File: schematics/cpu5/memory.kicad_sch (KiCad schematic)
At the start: 0 parts

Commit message: Multithread + paging!
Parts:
- added INTERNAL_ADDRESS_CONN2: Conn_01x16, Connector_PinHeader_2.54mm:PinHeader_1x16_P2.54mm_Vertical, symbol Connector_Generic:Conn_01x16
- added INTERNAL_DATA_CONN4, INTERNAL_DATA_CONN5: Conn_01x08, Connector_PinHeader_2.54mm:PinHeader_1x08_P2.54mm_Vertical, symbol Connector_Generic:Conn_01x08
- added ML8: 74LS574, Package_DIP:DIP-20_W7.62mm, symbol 7400_ice:74LS574
- added U100: CY62256-70PC, Package_DIP:DIP-28_W15.24mm, symbol Memory_RAM:CY62256-70PC
- added U101: 74LS04, Package_DIP:DIP-14_W7.62mm, symbol 7400_ice:74LS04
- added U102, U108: 74LS02, Package_DIP:DIP-14_W7.62mm, symbol 7400_ice:74LS02
- added U103, U104, U105, U106, U107, U115, U116, U118, U119, U94: 74LS541, Package_DIP:DIP-20_W7.62mm, symbol 7400_ice:74LS541
- added U109, U112, U113, U95: 74LS32, Package_DIP:DIP-14_W7.62mm, symbol 7400_ice:74LS32
- added U110, U111: AT28C64-20PI, Package_DIP:DIP-28_W7.62mm, symbol at28c64:AT28C64-20PI
- added U114, U117, U96: 74LS138, Package_DIP:DIP-16_W7.62mm, symbol 7400_ice:74LS138
- added U120: AS6C4008-55PCN, Package_DIP:DIP-32_W15.24mm, symbol Memory_RAM:AS6C4008-55PCN
- added U97: 74LS00, Package_DIP:DIP-14_W7.62mm, symbol 7400_ice:74LS00
- added U98: 28C256, Package_DIP:DIP-28_W15.24mm, symbol Memory_EEPROM:28C256
- added U99: 74LS08, Package_DIP:DIP-14_W7.62mm, symbol 7400_ice:74LS08
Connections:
- new net: U95.3 (Y1), U95.9 (A3)
- new net: U101.5 (A2), U95.13 (B4), U95.8 (Y3), U96.5 (Enable2_bar)
- new net: U95.10 (B3), U95.6 (Y2)
- new net: U109.3 (Y1), U112.13 (B4), U112.9 (A3)
- new net: U101.2 (Y0), U95.12 (A4)
- new net: U110.22 (/OE), U99.8 (Y3)
- new net: U102.5 (A2), U109.8 (Y3)
- new net: U109.10 (B3), U109.11 (Y4)
- new net: U109.6 (Y2), U112.1 (A1), U112.5 (B2)
- new net: U109.2 (B1), U109.5 (B2), U96.12 (Y3)
- new net: U114.5 (Enable2_bar), U96.13 (Y2)
- new net: U96.14 (Y1), U99.2 (B1)
- new net: U96.15 (Y0), U99.1 (A1)
- new net: U108.1 (Y1), U113.2 (B1)
- new net: U102.9 (B3), U113.3 (Y1)
- new net: U102.13 (Y4), U109.13 (B4)
- new net: U114.13 (Y2), U117.5 (Enable2_bar)
- new net: U115.1 (OE1_bar), U97.6 (Y2)
- new net: U101.12 (Y5), U109.4 (A2)
- new net: U111.22 (/OE), U99.6 (Y2)
- new net: U116.1 (OE1_bar), U97.11 (Y4)
- new net: ML8.11 (CLK), U102.1 (Y1)
- new net +5V: ML8.20 (VCC), U100.28 (VCC), U101.14 (VCC), U102.14 (VCC), U103.20 (VCC), U104.20 (VCC), U105.20 (VCC), U106.20 (VCC), U107.20 (VCC), U108.14 (VCC), U109.14 (VCC), U110.28 (VCC), U111.28 (VCC), U112.14 (VCC), U113.14 (VCC), U114.16 (VCC), U114.6 (Enable3), U115.20 (VCC), U116.20 (VCC), U117.16 (VCC), U117.6 (Enable3), U118.20 (VCC), U119.20 (VCC), U120.32 (VCC), U94.20 (VCC), U95.14 (VCC), U96.16 (VCC), U96.6 (Enable3), U97.14 (VCC), U98.27 (~{WE}), U98.28 (VCC), U99.14 (VCC)
- new net ADDR0: INTERNAL_ADDRESS_CONN2.1 (Pin_1), U100.10 (A0), U104.2 (A0), U117.1 (A0), U120.12 (A0), U98.10 (A0)
- new net ADDR1: INTERNAL_ADDRESS_CONN2.2 (Pin_2), U100.9 (A1), U104.3 (A1), U117.2 (A1), U120.11 (A1), U98.9 (A1)
- new net ADDR10: INTERNAL_ADDRESS_CONN2.11 (Pin_11), U100.21 (A10), U105.4 (A2), U114.1 (A0), U120.23 (A10), U98.21 (A10)
- new net ADDR11: INTERNAL_ADDRESS_CONN2.12 (Pin_12), U100.23 (A11), U105.5 (A3), U114.2 (A1), U120.25 (A11), U98.23 (A11)
- new net ADDR12: INTERNAL_ADDRESS_CONN2.13 (Pin_13), U101.13 (A5), U106.2 (A0), U109.1 (A1), U94.2 (A0)
- new net ADDR13: INTERNAL_ADDRESS_CONN2.14 (Pin_14), U106.3 (A1), U94.3 (A1)
- new net ADDR14: INTERNAL_ADDRESS_CONN2.15 (Pin_15), U106.4 (A2), U94.4 (A2)
- new net ADDR15: INTERNAL_ADDRESS_CONN2.16 (Pin_16), U106.5 (A3), U94.5 (A3)
- new net ADDR2: INTERNAL_ADDRESS_CONN2.3 (Pin_3), U100.8 (A2), U104.4 (A2), U117.3 (A2), U120.10 (A2), U98.8 (A2)
- new net ADDR3: INTERNAL_ADDRESS_CONN2.4 (Pin_4), U100.7 (A3), U104.5 (A3), U120.9 (A3), U98.7 (A3)
- new net ADDR4: INTERNAL_ADDRESS_CONN2.5 (Pin_5), U100.6 (A4), U104.6 (A4), U120.8 (A4), U98.6 (A4)
- new net ADDR5: INTERNAL_ADDRESS_CONN2.6 (Pin_6), U100.5 (A5), U104.7 (A5), U120.7 (A5), U98.5 (A5)
- new net ADDR6: INTERNAL_ADDRESS_CONN2.7 (Pin_7), U100.4 (A6), U104.8 (A6), U120.6 (A6), U98.4 (A6)
- new net ADDR7: INTERNAL_ADDRESS_CONN2.8 (Pin_8), U100.3 (A7), U104.9 (A7), U120.5 (A7), U98.3 (A7)
- new net ADDR8: INTERNAL_ADDRESS_CONN2.9 (Pin_9), U100.25 (A8), U105.2 (A0), U120.27 (A8), U98.25 (A8)
- new net ADDR9: INTERNAL_ADDRESS_CONN2.10 (Pin_10), U100.24 (A9), U105.3 (A1), U120.26 (A9), U98.24 (A9)
- new net DATA0: INTERNAL_DATA_CONN4.1 (Pin_1), ML8.2 (D0), U100.11 (D0), U115.2 (A0), U116.2 (A0), U118.18 (Y0), U119.18 (Y0), U120.13 (D0), U98.11 (D0)
- new net DATA1: INTERNAL_DATA_CONN4.2 (Pin_2), ML8.3 (D1), U100.12 (D1), U115.3 (A1), U116.3 (A1), U118.17 (Y1), U119.17 (Y1), U120.14 (D1), U98.12 (D1)
- new net DATA2: INTERNAL_DATA_CONN4.3 (Pin_3), ML8.4 (D2), U100.13 (D2), U115.4 (A2), U116.4 (A2), U118.16 (Y2), U119.16 (Y2), U120.15 (D2), U98.13 (D2)
- new net DATA3: INTERNAL_DATA_CONN4.4 (Pin_4), ML8.5 (D3), U100.15 (D3), U115.5 (A3), U116.5 (A3), U118.15 (Y3), U119.15 (Y3), U120.17 (D3), U98.15 (D3)
- new net DATA4: INTERNAL_DATA_CONN4.5 (Pin_5), ML8.6 (D4), U100.16 (D4), U115.6 (A4), U116.6 (A4), U118.14 (Y4), U119.14 (Y4), U120.18 (D4), U98.16 (D4)
- new net DATA5: INTERNAL_DATA_CONN4.6 (Pin_6), ML8.7 (D5), U100.17 (D5), U115.7 (A5), U116.7 (A5), U118.13 (Y5), U119.13 (Y5), U120.19 (D5), U98.17 (D5)
- new net DATA6: INTERNAL_DATA_CONN4.7 (Pin_7), ML8.8 (D6), U100.18 (D6), U115.8 (A6), U116.8 (A6), U118.12 (Y6), U119.12 (Y6), U120.20 (D6), U98.18 (D6)
- new net DATA7: INTERNAL_DATA_CONN4.8 (Pin_8), ML8.9 (D7), U100.19 (D7), U115.9 (A7), U116.9 (A7), U118.11 (Y7), U119.11 (Y7), U120.21 (D7), U98.19 (D7)
- new net DBG_SEL_RAM: U100.20 (~{CS}), U95.11 (Y4)
- new net DBG_SEL_ROM: U98.20 (~{CS}), U99.3 (Y1)
- new net EADDR12: U100.2 (A12), U103.18 (Y0), U114.3 (A2), U120.4 (A12), U94.18 (Y0), U98.2 (A12)
- new net EADDR13: U100.26 (A13), U103.17 (Y1), U120.28 (A13), U94.17 (Y1), U96.1 (A0), U98.26 (A13)
- new net EADDR14: U100.1 (A14), U103.16 (Y2), U120.3 (A14), U94.16 (Y2), U96.2 (A1)
- new net EADDR15: U101.1 (A0), U103.15 (Y3), U120.31 (A15), U94.15 (Y3), U96.3 (A2)
- new net EADDR16: U103.14 (Y4), U120.2 (A16), U94.14 (Y4), U95.1 (A1)
- new net EADDR17: U103.13 (Y5), U120.30 (A17), U94.13 (Y5), U95.2 (B1)
- new net EADDR18: U103.12 (Y6), U120.1 (A18), U94.12 (Y6), U95.4 (A2)
- new net EADDR19: U103.11 (Y7), U94.11 (Y7), U95.5 (B2)
- new net EXTRAM_SEL: U101.6 (Y2), U120.22 (~{CE})
- new net GND: ML8.10 (GND), U100.14 (GND), U101.7 (GND), U102.7 (GND), U103.10 (GND), U103.19 (OE2_bar), U104.10 (GND), U104.19 (OE2_bar), U105.10 (GND), U105.19 (OE2_bar), U105.6 (A4), U105.7 (A5), U105.8 (A6), U105.9 (A7), U106.10 (GND), U106.19 (OE2_bar), U107.10 (GND), U107.19 (OE2_bar), U107.6 (A4), U107.7 (A5), U107.8 (A6), U107.9 (A7), U108.7 (GND), U109.7 (GND), U110.14 (GND), U110.2 (A12), U110.20 (/CE), U111.14 (GND), U111.2 (A12), U111.20 (/CE), U112.7 (GND), U113.7 (GND), U114.4 (Enable1_bar), U114.8 (GND), U115.10 (GND), U115.19 (OE2_bar), U116.10 (GND), U116.19 (OE2_bar), U117.4 (Enable1_bar), U117.8 (GND), U118.10 (GND), U118.19 (OE2_bar), U119.10 (GND), U119.19 (OE2_bar), U120.16 (VSS), U94.10 (GND), U94.19 (OE2_bar), U94.6 (A4), U94.7 (A5), U94.8 (A6), U94.9 (A7), U95.7 (GND), U96.4 (Enable1_bar), U96.8 (GND), U97.7 (GND), U98.1 (A14), U98.14 (GND), U99.7 (GND)
- new net MREAD: INTERNAL_DATA_CONN5.2 (Pin_2), U100.22 (~{OE}), U112.10 (B3), U112.2 (B1), U120.24 (~{OE}), U98.22 (~{OE})
- new net MWRITE: INTERNAL_DATA_CONN5.1 (Pin_1), U100.27 (~{WE}), U102.12 (B4), U102.2 (A1), U108.3 (B1), U112.12 (A4), U112.4 (A2), U120.29 (~{WE})
- new net PGE: U102.4 (Y2), U102.8 (A3), U104.1 (OE1_bar), U105.1 (OE1_bar), U94.1 (OE1_bar)
- new net PGE_bar: ML8.1 (OE_bar), U102.10 (Y3), U102.6 (B2), U103.1 (OE1_bar), U106.1 (OE1_bar), U107.1 (OE1_bar), U97.13 (B4), U97.5 (B2), U99.10 (B3), U99.5 (B2)
- new net READ_TLB: U112.8 (Y3), U118.1 (OE1_bar), U97.4 (A2), U99.9 (A3)
- new net READ_TLBF: U112.3 (Y1), U119.1 (OE1_bar), U97.12 (A4), U99.4 (A2)
- new net RESET_PAGING_SEL: U102.11 (A4), U117.15 (Y0)
- new net RESET_bar: U109.9 (A3)
- new net SEL_TLB_INDEX: U102.3 (B1), U117.13 (Y2)
- new net SELa_PGdis: INTERNAL_DATA_CONN5.3 (Pin_3), U109.12 (A4)
- new net SET_PAGING_SEL: U108.2 (A1), U117.14 (Y1)
- new net TLBA0: U104.18 (Y0), U106.18 (Y0), U110.10 (A0), U111.10 (A0)
- new net TLBA1: U104.17 (Y1), U106.17 (Y1), U110.9 (A1), U111.9 (A1)
- new net TLBA10: U105.16 (Y2), U107.16 (Y2), U110.21 (A10), U111.21 (A10)
- new net TLBA11: U105.15 (Y3), U107.15 (Y3), U110.23 (A11), U111.23 (A11)
- new net TLBA2: U104.16 (Y2), U106.16 (Y2), U110.8 (A2), U111.8 (A2)
- new net TLBA3: U104.15 (Y3), U106.15 (Y3), U110.7 (A3), U111.7 (A3)
- new net TLBA4: U104.14 (Y4), U106.14 (Y4), U110.6 (A4), U111.6 (A4)
- new net TLBA5: U104.13 (Y5), U106.13 (Y5), U110.5 (A5), U111.5 (A5)
- new net TLBA6: U104.12 (Y6), U106.12 (Y6), U110.4 (A6), U111.4 (A6)
- new net TLBA7: U104.11 (Y7), U106.11 (Y7), U110.3 (A7), U111.3 (A7)
- new net TLBA8: U105.18 (Y0), U107.18 (Y0), U110.25 (A8), U111.25 (A8)
- new net TLBA9: U105.17 (Y1), U107.17 (Y1), U110.24 (A9), U111.24 (A9)
- new net TLBD0: U103.2 (A0), U110.11 (D0), U115.18 (Y0), U118.2 (A0)
- new net TLBD1: U103.3 (A1), U110.12 (D1), U115.17 (Y1), U118.3 (A1)
- new net TLBD2: U103.4 (A2), U110.13 (D2), U115.16 (Y2), U118.4 (A2)
- new net TLBD3: U103.5 (A3), U110.15 (D3), U115.15 (Y3), U118.5 (A3)
- new net TLBD4: U103.6 (A4), U110.16 (D4), U115.14 (Y4), U118.6 (A4)
- new net TLBD5: U103.7 (A5), U110.17 (D5), U115.13 (Y5), U118.7 (A5)
- new net TLBD6: U103.8 (A6), U110.18 (D6), U115.12 (Y6), U118.8 (A6)
- new net TLBD7: U103.9 (A7), U110.19 (D7), U115.11 (Y7), U118.9 (A7)
- new net TLBFD0: U111.11 (D0), U116.18 (Y0), U119.2 (A0)
- new net TLBFD1: U111.12 (D1), U116.17 (Y1), U119.3 (A1)
- new net TLBFD2: U111.13 (D2), U116.16 (Y2), U119.4 (A2)
- new net TLBFD3: U111.15 (D3), U116.15 (Y3), U119.5 (A3)
- new net TLBFD4: U111.16 (D4), U116.14 (Y4), U119.6 (A4)
- new net TLBFD5: U111.17 (D5), U116.13 (Y5), U119.7 (A5)
- new net TLBFD6: U111.18 (D6), U116.12 (Y6), U119.8 (A6)
- new net TLBFD7: U111.19 (D7), U116.11 (Y7), U119.9 (A7)
- new net TLBi0: ML8.19 (Y0), U106.6 (A4)
- new net TLBi1: ML8.18 (Y1), U106.7 (A5)
- new net TLBi2: ML8.17 (Y2), U106.8 (A6)
- new net TLBi3: ML8.16 (Y3), U106.9 (A7)
- new net TLBi4: ML8.15 (Y4), U107.2 (A0)
- new net TLBi5: ML8.14 (Y5), U107.3 (A1)
- new net TLBi6: ML8.13 (Y6), U107.4 (A2)
- new net TLBi7: ML8.12 (Y7), U107.5 (A3)
- new net WRITE_TLB: U110.27 (/WE), U112.11 (Y4)
- new net WRITE_TLBF: U111.27 (/WE), U112.6 (Y2)
- new net ei: INTERNAL_DATA_CONN5.4 (Pin_4), U113.1 (A1)
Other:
- note added: "0x0000-0x3fff"
- note added: "0x4000-0x5fff"
- note added: "0x4800"
- note added: "0x4800-0x4bff"
- note added: "0x4801"
- note added: "0x4802"
- note added: "0x6000-0x7fff"

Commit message: start faults
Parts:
- added ML10, ML11, ML9: 74LS574, Package_DIP:DIP-20_W7.62mm, symbol 7400_ice:74LS574
- added U121: 74LS32, Package_DIP:DIP-14_W7.62mm, symbol 7400_ice:74LS32
- added U123: 74LS08, Package_DIP:DIP-14_W7.62mm, symbol 7400_ice:74LS08
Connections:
- net +5V: now also ML10.20 (VCC), ML11.20 (VCC), ML9.20 (VCC), U121.14 (VCC), U123.14 (VCC)
- net ADDR0: now also ML9.2 (D0)
- net ADDR1: now also ML9.3 (D1)
- net ADDR10: now also ML10.4 (D2)
- net ADDR11: now also ML10.5 (D3)
- net ADDR2: now also ML9.4 (D2)
- net ADDR3: now also ML9.5 (D3)
- net ADDR4: now also ML9.6 (D4)
- net ADDR5: now also ML9.7 (D5)
- net ADDR6: now also ML9.8 (D6)
- net ADDR7: now also ML9.9 (D7)
- net ADDR8: now also ML10.2 (D0)
- net ADDR9: now also ML10.3 (D1)
- net DATA0: now also ML10.19 (Y0), ML11.19 (Y0), ML9.19 (Y0)
- net DATA1: now also ML10.18 (Y1), ML11.18 (Y1), ML9.18 (Y1)
- net DATA2: now also ML10.17 (Y2), ML11.17 (Y2), ML9.17 (Y2)
- net DATA3: now also ML10.16 (Y3), ML11.16 (Y3), ML9.16 (Y3)
- net DATA4: now also ML10.15 (Y4), ML11.15 (Y4), ML9.15 (Y4)
- net DATA5: now also ML10.14 (Y5), ML11.14 (Y5), ML9.14 (Y5)
- net DATA6: now also ML10.13 (Y6), ML11.13 (Y6), ML9.13 (Y6)
- net DATA7: now also ML10.12 (Y7), ML11.12 (Y7), ML9.12 (Y7)
- net EADDR12: now also ML10.6 (D4)
- net EADDR13: now also ML10.7 (D5)
- net EADDR14: now also ML10.8 (D6)
- net EADDR15: now also ML10.9 (D7)
- net EADDR16: now also ML11.2 (D0)
- net EADDR17: now also ML11.3 (D1)
- net EADDR18: now also ML11.4 (D2)
- net EADDR19: now also ML11.5 (D3)
- net GND: now also ML8.1 (OE_bar), ML10.10 (GND), ML11.10 (GND), ML9.10 (GND), U121.7 (GND), U123.7 (GND)
- net MREAD: now also U108.12 (B4), U121.10 (B3), U121.12 (A4), U121.2 (B1), U121.5 (B2); no longer U100.22 (~{OE}), U120.24 (~{OE}), U98.22 (~{OE})
- net MWRITE: now also U108.6 (B2), U113.12 (A4); no longer U100.27 (~{WE}), U120.29 (~{WE})
- net PGE: now also U99.13 (B4), U123.2 (B1)
- net PGE_bar: no longer ML8.1 (OE_bar)
- net TLBFD0: now also U108.11 (A4), ML11.6 (D4)
- net TLBFD1: now also U108.5 (A2), ML11.7 (D5)
- net TLBFD2: now also ML11.8 (D6)
- net TLBFD3: now also ML11.9 (D7)
- net at U108.4 (Y2): now also U99.12 (A4)
- net at U99.11 (Y4): now also U113.10 (B3), U113.13 (B4)
- net MWRITE_f: now reaches U113.11 (Y4)
- net MWRITE_f: now also U100.27 (~{WE}), U120.29 (~{WE})
- net RD_FLT_1: now reaches U117.10 (Y5)
- net RD_FLT_1: now also U121.9 (A3)
- net RD_FLT_0: now reaches U117.11 (Y4)
- net RD_FLT_0: now also U121.4 (A2)
- net RD_FLT_2: now reaches U117.9 (Y6)
- net RD_FLT_2: now also U121.1 (A1)
- net at U108.13 (Y4): now also U123.1 (A1)
- net MMU_FAULT: now reaches U113.9 (A3)
- net MMU_FAULT: now also ML10.11 (CLK), ML11.11 (CLK), ML9.11 (CLK), U121.13 (B4), U123.3 (Y1)
- new net: ML10.1 (OE_bar), U121.8 (Y3)
- new net: ML11.1 (OE_bar), U121.3 (Y1)
- new net: ML9.1 (OE_bar), U121.6 (Y2)
- new net MREAD_f: U100.22 (~{OE}), U120.24 (~{OE}), U121.11 (Y4), U98.22 (~{OE})
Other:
- note added: "0x4803"
- note added: "0x4804"
- note added: "0x4805"
- note added: "0x4806"
- moved on the sheet: U101B, U101D, U101E, U108B, U108D, U113C, U113D, U97C, U99D

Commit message: faults seem to work
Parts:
- added U131: 74LS74, Package_DIP:DIP-14_W7.62mm, symbol 7400_ice:74LS74
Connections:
- net +5V: now also U131.14 (VCC), U131.4 (nS1)
- net GND: now also U131.7 (GND)
- net MMU_FAULT: now also U113.8 (Y3); no longer U113.9 (A3), U121.13 (B4), U123.3 (Y1)
- net PGE: now also U131.5 (Q1); no longer U102.4 (Y2), U102.8 (A3)
- net PGE_bar: now also U131.6 (nQ1); no longer U102.10 (Y3), U102.6 (B2)
- net RD_FLT_0: now also U117.10 (Y5); no longer U117.11 (Y4)
- net RD_FLT_1: now also U117.9 (Y6); no longer U117.10 (Y5)
- net RD_FLT_2: now also U117.7 (Y7); no longer U117.9 (Y6)
- net SET_PAGING_SEL: now also U123.5 (B2), U123.9 (A3)
- net at U113.10 (B3), U113.13 (B4): now also U123.8 (Y3); no longer U99.11 (Y4)
- net at U123.4 (A2): now also U123.3 (Y1)
- net at U123.6 (Y2): now also U113.9 (A3), U121.13 (B4)
- net at U123.10 (B3): now also U99.11 (Y4)
- new net: U102.4 (Y2), U102.8 (A3), U131.2 (D1)
- new net: U102.10 (Y3), U102.6 (B2)
- new net RESET: U131.1 (nR1)
- new net start_phase: U131.3 (Clk1)
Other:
- note added: "0x4807"
- moved on the sheet: U101B, U101D, U101E, U108B, U108D, U113C, U113D, U121D, U123A, U123B, U123C, U123D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

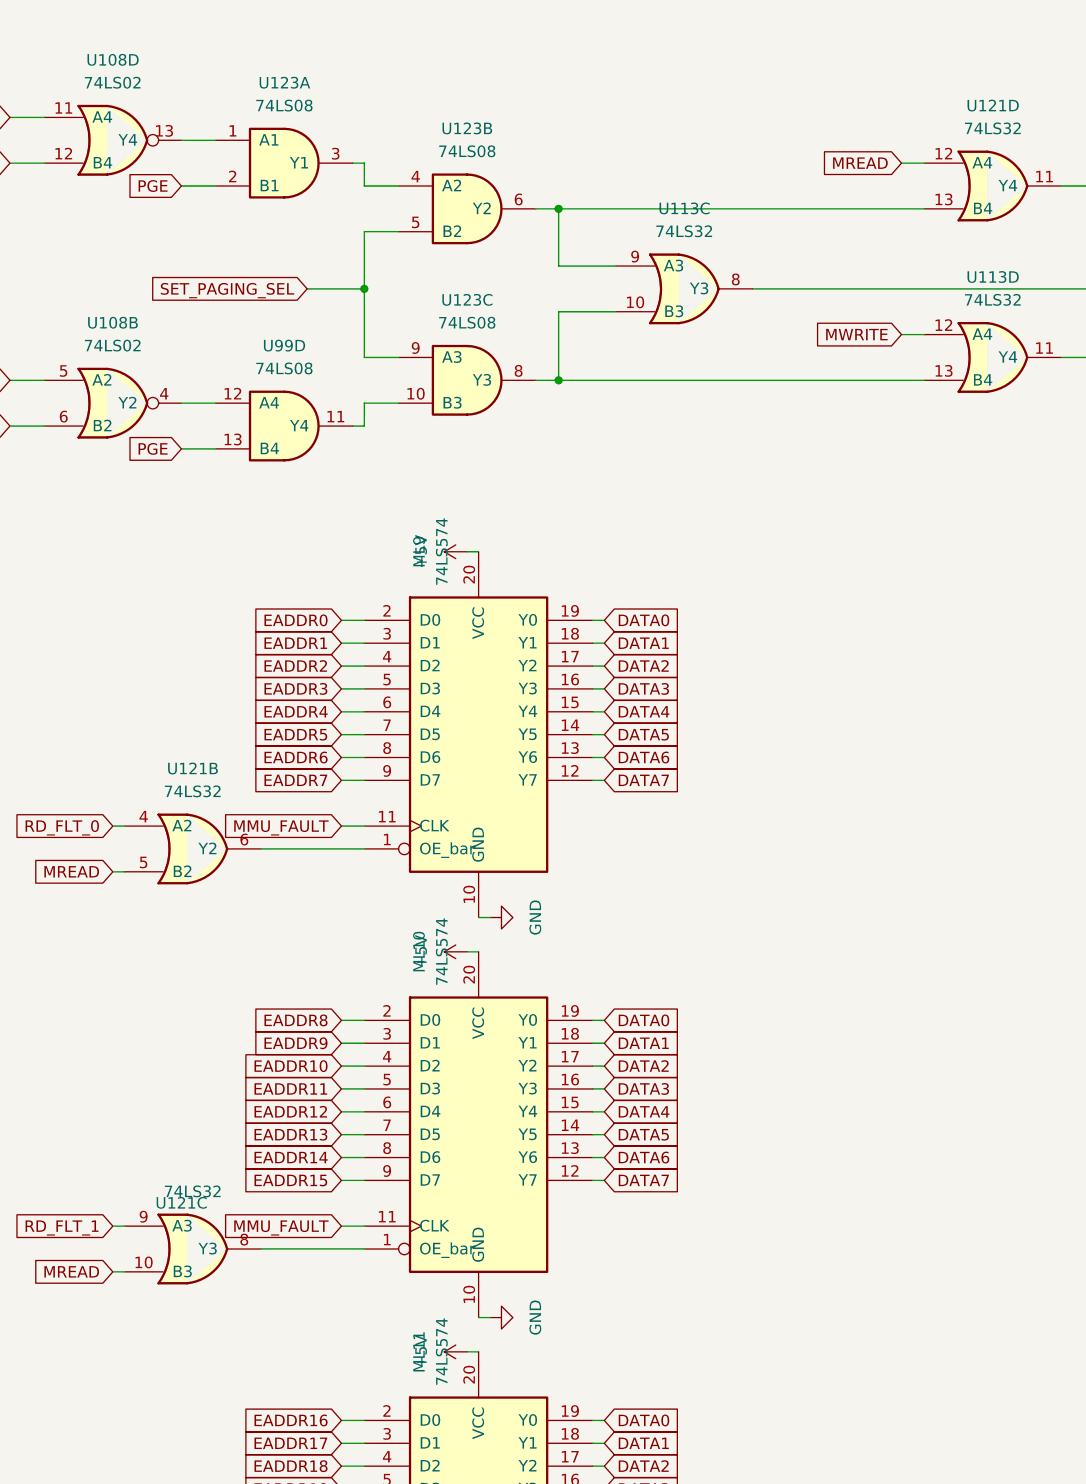
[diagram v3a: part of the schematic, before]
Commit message: Page faults work
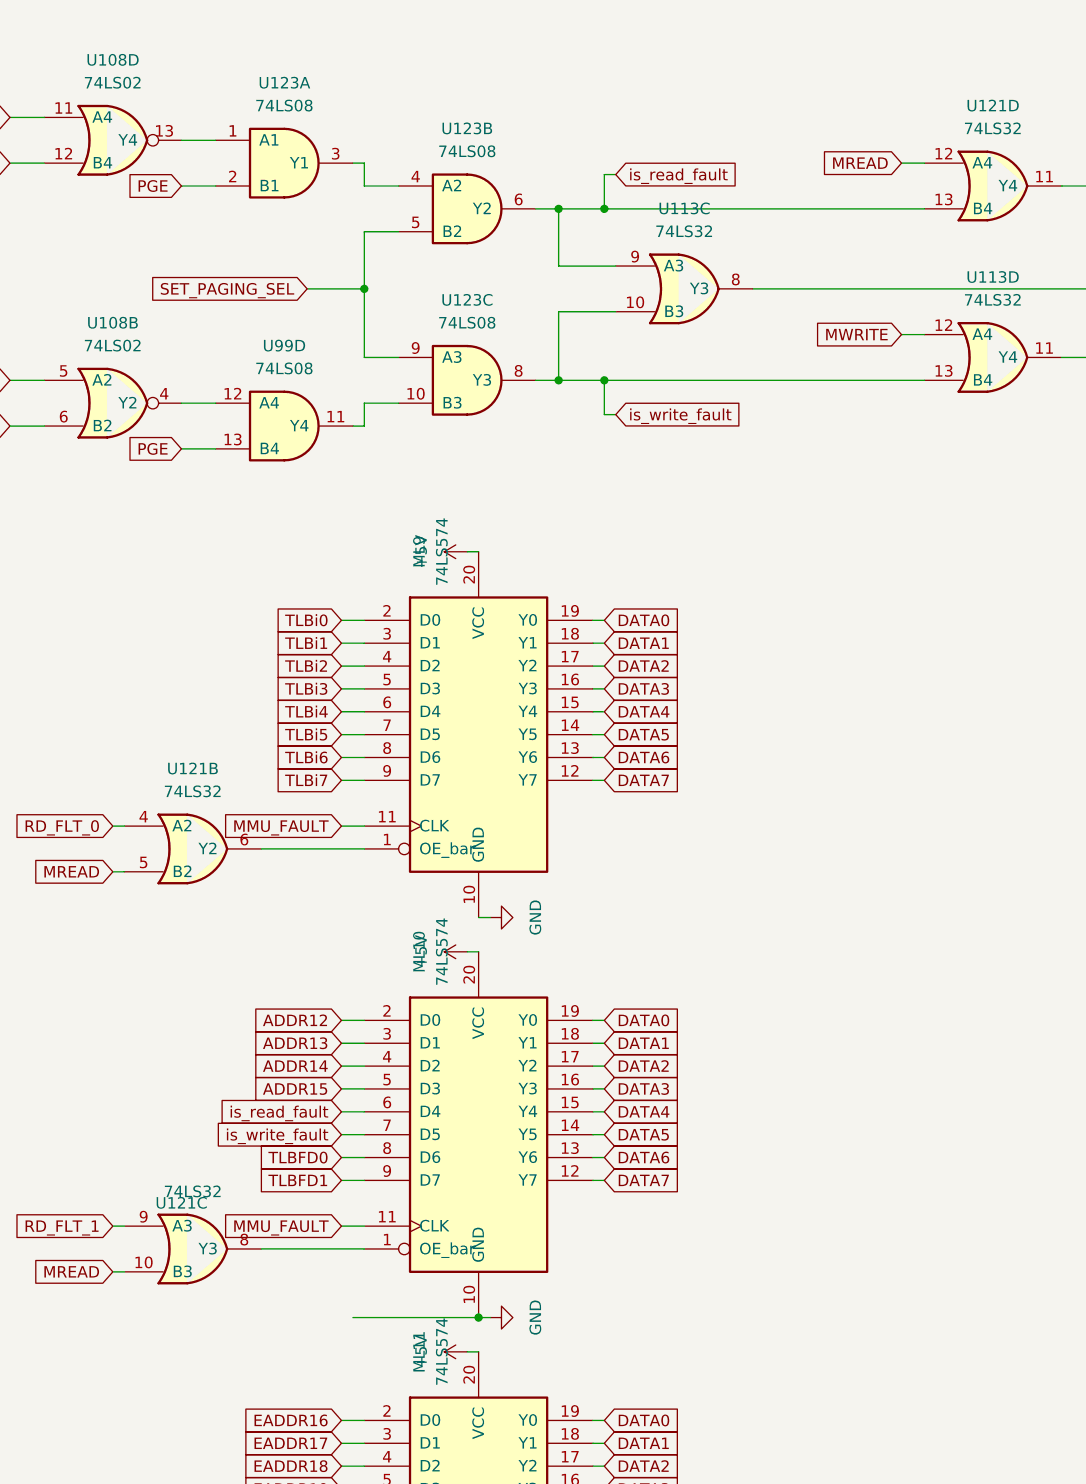
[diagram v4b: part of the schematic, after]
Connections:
- net ADDR0: no longer ML9.2 (D0)
- net ADDR1: no longer ML9.3 (D1)
- net ADDR10: no longer ML10.4 (D2)
- net ADDR11: no longer ML10.5 (D3)
- net ADDR12: now also ML10.2 (D0)
- net ADDR13: now also ML10.3 (D1)
- net ADDR14: now also ML10.4 (D2)
- net ADDR15: now also ML10.5 (D3)
- net ADDR2: no longer ML9.4 (D2)
- net ADDR3: no longer ML9.5 (D3)
- net ADDR4: no longer ML9.6 (D4)
- net ADDR5: no longer ML9.7 (D5)
- net ADDR6: no longer ML9.8 (D6)
- net ADDR7: no longer ML9.9 (D7)
- net ADDR8: no longer ML10.2 (D0)
- net ADDR9: no longer ML10.3 (D1)
- net EADDR12: no longer ML10.6 (D4)
- net EADDR13: no longer ML10.7 (D5)
- net EADDR14: no longer ML10.8 (D6)
- net EADDR15: no longer ML10.9 (D7)
- net TLBFD0: now also ML10.8 (D6)
- net TLBFD1: now also ML10.9 (D7)
- net TLBi0: now also ML9.2 (D0)
- net TLBi1: now also ML9.3 (D1)
- net TLBi2: now also ML9.4 (D2)
- net TLBi3: now also ML9.5 (D3)
- net TLBi4: now also ML9.6 (D4)
- net TLBi5: now also ML9.7 (D5)
- net TLBi6: now also ML9.8 (D6)
- net TLBi7: now also ML9.9 (D7)
- net is_read_fault: now reaches U113.9 (A3), U121.13 (B4), U123.6 (Y2)
- net is_read_fault: now also ML10.6 (D4)
- net is_write_fault: now reaches U113.10 (B3), U113.13 (B4), U123.8 (Y3)
- net is_write_fault: now also ML10.7 (D5)

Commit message: perf experiments
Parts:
- U100: VerilogCode at28c256_rom #(.ROM_INDEX(-1)) U(.A(`A), .D(`D), .nCE(nCS),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 -> at28c256_rom #(.ROM_INDEX(11)) U(.A(`A), .D(`D), .nCE(nCS),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
- U110: VerilogCode at28c64_rom #(.ROM_INDEX(-1)) U(.A(`A), .D(`D), .nCE(_CE), 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 -> at28c64_rom #(.ROM_INDEX(12)) U(.A(`A), .D(`D), .nCE(_CE), 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
- U111: VerilogCode at28c64_rom #(.ROM_INDEX(-1)) U(.A(`A), .D(`D), .nCE(_CE), 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 -> at28c64_rom #(.ROM_INDEX(13)) U(.A(`A), .D(`D), .nCE(_CE), 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
- U120: VerilogCode ram_512 #(.ROM_INDEX(-1)) U(.A(`A), .D(`D), .nCE(nCE), .nOE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 -> ram_512 #(.ROM_INDEX(10)) U(.A(`A), .D(`D), .nCE(nCE), .nOE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
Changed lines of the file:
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@@
       (effects (font (size 1.27 1.27)) hide)
     )
-    (property "VerilogCode" "at28c256_rom #(.ROM_INDEX(-1)) U(.A(`A), .D(`D), .nCE(nCS), .nOE(nOE), .nWE(nWE));" (id 5) (at 242.57 198.12 0)
+    (property "VerilogCode" "at28c256_rom #(.ROM_INDEX(11)) U(.A(`A), .D(`D), .nCE(nCS), .nOE(nOE), .nWE(nWE));" (id 5) (at 242.57 198.12 0)
       (effects (font (size 1.27 1.27)) hide)
     )
@@
       (effects (font (size 1.27 1.27)) hide)
     )
-    (property "VerilogCode" "at28c64_rom #(.ROM_INDEX(-1)) U(.A(`A), .D(`D), .nCE(_CE), .nOE(_OE), .nWE(_WE));" (id 5) (at 226.06 295.91 0)
+    (property "VerilogCode" "at28c64_rom #(.ROM_INDEX(12)) U(.A(`A), .D(`D), .nCE(_CE), .nOE(_OE), .nWE(_WE));" (id 5) (at 226.06 295.91 0)
       (effects (font (size 1.27 1.27)) hide)
     )
@@
       (effects (font (size 1.27 1.27)) hide)
     )
-    (property "VerilogCode" "at28c64_rom #(.ROM_INDEX(-1)) U(.A(`A), .D(`D), .nCE(_CE), .nOE(_OE), .nWE(_WE));" (id 5) (at 226.06 349.25 0)
+    (property "VerilogCode" "at28c64_rom #(.ROM_INDEX(13)) U(.A(`A), .D(`D), .nCE(_CE), .nOE(_OE), .nWE(_WE));" (id 5) (at 226.06 349.25 0)
       (effects (font (size 1.27 1.27)) hide)
     )
@@
       (effects (font (size 1.27 1.27)) hide)
     )
-    (property "VerilogCode" "ram_512 #(.ROM_INDEX(-1)) U(.A(`A), .D(`D), .nCE(nCE), .nOE(nOE), .nWE(nWE));" (id 5) (at 396.24 100.33 0)
-      (effects (font (size 1.27 1.27)) hide)
-    )
+    (property "VerilogCode" "ram_512 #(.ROM_INDEX(10)) U(.A(`A), .D(`D), .nCE(nCE), .nOE(nOE), .nWE(nWE));" (id 5) (at 396.24 100.33 0)
+      (effects (font (size 1.27 1.27)) hide)
+    )
